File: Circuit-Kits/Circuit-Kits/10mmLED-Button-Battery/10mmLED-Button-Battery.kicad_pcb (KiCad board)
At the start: 2 copper layers, 41.8 x 34.2 mm, 9 parts, among them SW1 Pushbutton

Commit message: Release 10mmLED version 1.0.
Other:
- board text added: "Assembly Information 10mmLED-Button-Battery v1.3"
- board text removed: "Assembly Information LegoLED-Button-Battery v1.3"
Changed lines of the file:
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@@
     (effects (font (size 1.016 1.016) (thickness 0.1524)) (justify right))
   )
-  (gr_text "Assembly Information\nLegoLED-Button-Battery v1.3" (at 185.6232 81.6864) (layer F.Fab)
+  (gr_text "Assembly Information\n10mmLED-Button-Battery v1.3" (at 185.6232 81.6864) (layer F.Fab)
     (effects (font (size 1.016 1.016) (thickness 0.1524)) (justify right))
   )

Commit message: Release USB-Breakout-with-Reset v1.0 fix.
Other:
- board text added: "Crazy Circuit Kit 12/27/16"
- board text removed: "Rewire Circuit Kit 12/27/16"
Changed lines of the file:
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@@
   (gr_line (start 171.6024 114.554) (end 171.6024 115.3668) (layer Edge.Cuts) (width 0.1524))
   (gr_arc (start 175.26 115.316) (end 175.26 118.999) (angle 89.2151803) (layer Edge.Cuts) (width 0.1524))
-  (gr_text "Rewire Circuit Kit\n12/27/16" (at 185.6232 122.428) (layer F.Fab)
+  (gr_text "Crazy Circuit Kit\n12/27/16" (at 185.6232 122.428) (layer F.Fab)
     (effects (font (size 1.016 1.016) (thickness 0.1524)) (justify right))
   )

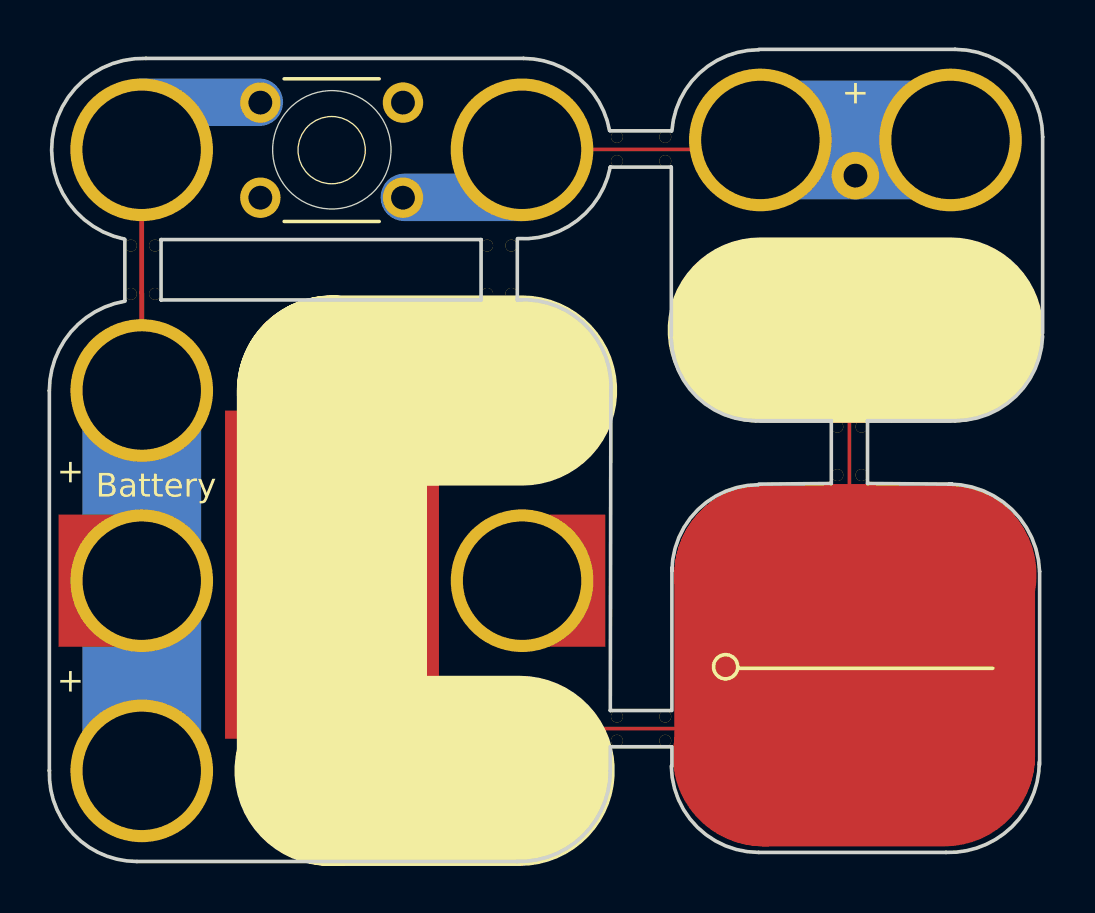
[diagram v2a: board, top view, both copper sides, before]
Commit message: Changed 10mm from 5mm pitch to 2.54mm pitch.
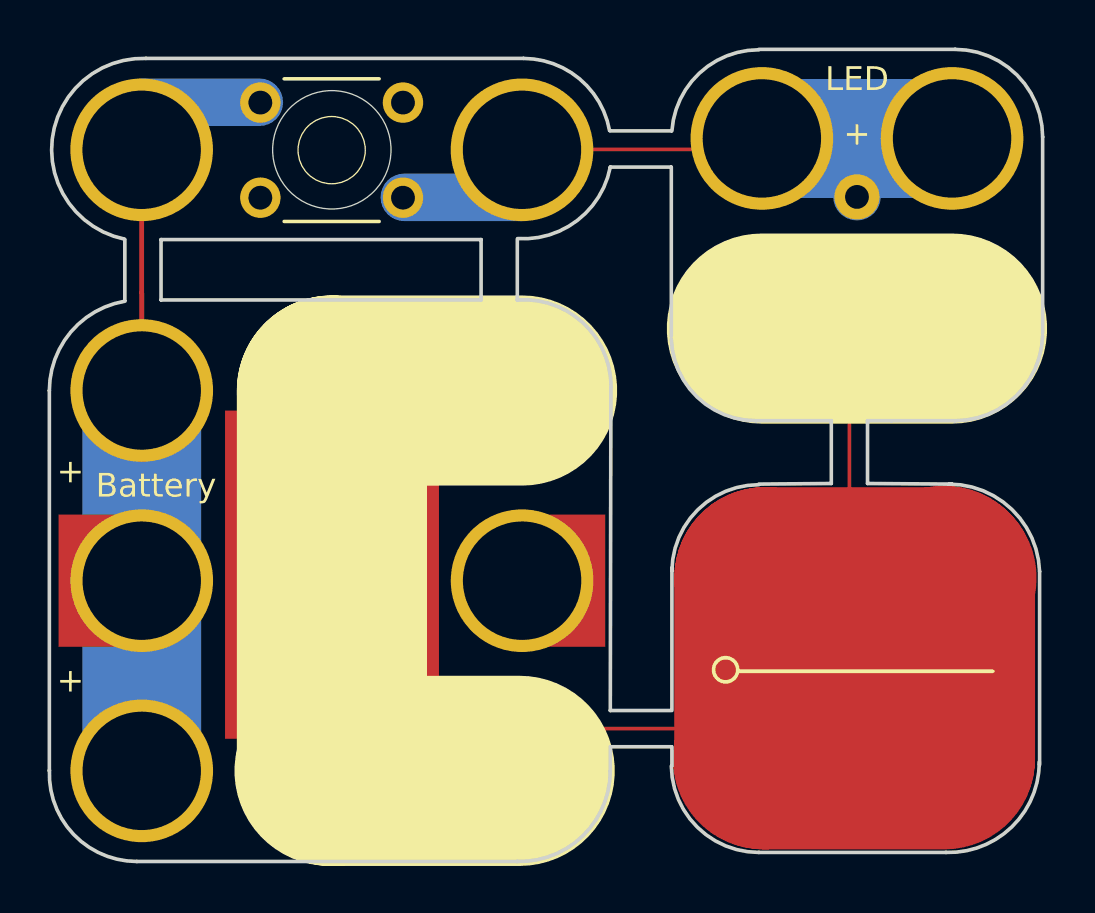
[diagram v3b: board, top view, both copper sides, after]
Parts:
- removed LED: Val**, Crazy_Circuits:LED-10MMD-5MMP-TH-2x2
- removed REF** (x4): TAB-20MIL-2x4-SNAP, Rewire_Circuits:TAB-20MIL-2x2-SNAP
- removed REF**: TAB-20MIL-2x2-SNAP, Rewire_Circuits:TAB-20MIL-2x2-SNAP
- added LED1: LED, Crazy_Circuits:LED-5MMD-2.5MMP-2x2, F.Cu at (183.4, 89.0)
- BT1: footprint Rewire_Circuits:CR2032-3x3-NO-ROTATE -> Crazy_Circuits:CR2032-3x3-NO-ROTATE
- SW1: footprint Rewire_Circuits:BUTTON-1x3-TH-OMRON-B3F-1XXX -> Crazy_Circuits:BUTTON-1x3-TH-OMRON-B3F-1XXX
- moved LOGO 0.13 mm to (179.3, 111.4)
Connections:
- net Net-(BT1-Pad+) renamed +3V
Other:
- board text added: "Assembly Information 10mmLED-Button-Battery v1.1"
- board text added: "Crazy Circuit Kit 1/12/17"
- board text removed: "Assembly Information 10mmLED-Button-Battery v1.3"
- board text removed: "Crazy Circuit Kit 12/27/16"

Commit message: Updated Circuit Kits.
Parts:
- added REF**: TAB-20MIL-2x4-SNAP, Crazy_Circuits:TAB-20MIL-2x2-SNAP, F.Cu at (59.5, 48.0)
- added REF**: TAB-20MIL-2x4-SNAP, Crazy_Circuits:TAB-20MIL-2x2-SNAP, F.Cu at (50.8, 59.7)
- added REF**: TAB-20MIL-2x4-SNAP, Crazy_Circuits:TAB-20MIL-2x2-SNAP, F.Cu at (29.8, 40.3)
- added REF**: TAB-20MIL-2x4-SNAP, Crazy_Circuits:TAB-20MIL-2x2-SNAP, F.Cu at (44.8, 40.3)
- added REF**: TAB-20MIL-2x4-SNAP, Crazy_Circuits:TAB-20MIL-2x2-SNAP, F.Cu at (50.8, 35.3)
- BT1: footprint Crazy_Circuits:CR2032-3x3-NO-ROTATE -> Crazy_Circuits:CR2032-3x3
- LED1: footprint Crazy_Circuits:LED-5MMD-2.5MMP-2x2 -> Crazy_Circuits:LED-2.54MM-TH-2x2
- moved LOGO 131.2 mm to (59.8, 57.2)
- moved BT1 131.2 mm to (45.8, 45.4)
- moved LED1 131.2 mm to (63.9, 34.8)
- moved SW1 131.2 mm to (29.8, 35.3)
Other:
- board text added: "Assembly Information 10mmLED-Button-Battery v1.2"
- board text added: "FABRICATION NOTES 1. THIS IS A 2 LAYER BOARD. 2. EXTERNAL LAYERS SHALL HAVE 1 OZ COPPER. 3. MATERIAL: FR4 AND 0.062 INCH +/- 10% THICK. 4. BOARDS SHALL BE ROHS COMPLIANT. 5. MANUFACTURE IN ACCORDANCE WITH IPC-6012 CLASS 2 6. MASK: BOTH SIDES OF THE BOARD SHALL HAVE SOLDER MASK (ANY COLOR) OVER BARE COPPER. 7. SILK: BOTH SIDES OF THE BOARD SHALL HAVE WHITE SILK. DO NOT PLACE SILK OVER BARE COPPER.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"
- board text removed: "Assembly Information 10mmLED-Button-Battery v1.1"
- board text removed: "Crazy Circuit Kit 1/12/17"

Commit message: Wave solder fixes for v1.3 10mmLED-Button-Battery kit
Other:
- board text removed: "Assembly Information 10mmLED-Button-Battery v1.2"
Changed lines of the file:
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@@
-(kicad_pcb (version 4) (host pcbnew 4.0.5-e0-6337~49~ubuntu16.04.1)
+(kicad_pcb (version 4) (host pcbnew 4.0.7-e2-6376~58~ubuntu16.04.1)
   (general
     (links 16)
     (no_connects 13)
-    (area 21.073553 25.908 68.258248 68.410647)
+    (area 21.073553 25.908 167.965359 182.0418)
     (thickness 1.6)
-    (drawings 48)
+    (drawings 47)
     (tracks 22)
     (zones 0)
@@
     (pad 1 thru_hole circle (at -0.508 1.016 180) (size 0.5 0.5) (drill 0.5) (layers *.Cu))
   )
-  (module Crazy_Circuits:LED-2.54MM-TH-2x2 (layer F.Cu)
-    (at 63.8556 34.8107 180)
-    (descr "LED 5mm round vertical")
-    (tags "LED 5mm round vertical")
-    (fp_text reference LED1 (at 4 -4 270) (layer F.Fab)
-      (effects (font (size 1 1) (thickness 0.15)))
-    )
-    (fp_text value LED (at 4 2.5 180) (layer F.SilkS)
-      (effects (font (size 1 1) (thickness 0.15)))
-    )
-    (fp_line (start 3.302 -7.366) (end 4.445 -7.366) (layer F.Fab) (width 0.0762))
-    (fp_arc (start 3.937 -3.81) (end 5.588 -6.731) (angle 301.0482285) (layer F.Fab) (width 0.0464))
-    (fp_line (start 2.286 -6.731) (end 5.588 -6.731) (layer F.Fab) (width 0.0464))
-    (fp_arc (start 0.195441 -0.199792) (end 0 3.8) (angle 84.2) (layer Edge.Cuts) (width 0.05))
-    (fp_line (start 11.8 -8) (end 11.8 0) (layer Edge.Cuts) (width 0.05))
-    (fp_line (start 0 -11.8) (end 8 -11.8) (layer Edge.Cuts) (width 0.05))
-    (fp_line (start 0 3.8) (end 8 3.8) (layer Edge.Cuts) (width 0.05))
-    (fp_line (start -3.8 -8) (end -3.8 0) (layer Edge.Cuts) (width 0.05))
-    (fp_arc (start 0.195441 -0.199792) (end 0 3.8) (angle 84.2) (layer F.Fab) (width 0.05))
-    (fp_line (start 11.8 -8) (end 11.8 0) (layer F.Fab) (width 0.05))
-    (fp_line (start 0 -11.8) (end 8 -11.8) (layer F.Fab) (width 0.05))
-    (fp_line (start 0 3.8) (end 8 3.8) (layer F.Fab) (width 0.05))
-    (fp_line (start -3.8 -8) (end -3.8 0) (layer F.Fab) (width 0.05))
-    (fp_line (start 4 -5.2) (end 4 -6.3) (layer B.Cu) (width 2))
-    (fp_line (start 8 -8) (end 0 -8) (layer B.Mask) (width 7))
-    (fp_text user + (at 4 0.2 180) (layer F.SilkS)
-      (effects (font (size 1 1) (thickness 0.15)))
-    )
-    (fp_line (start 0 -8) (end 8 -8) (layer F.SilkS) (width 8))
-    (fp_line (start 2.5 -6.23) (end 5.5 -6.23) (layer F.SilkS) (width 0.15))
-    (fp_line (start 8 -8) (end 0 -8) (layer B.Cu) (width 7))
-    (fp_line (start 8 0) (end 0 0) (layer B.Mask) (width 7))
-    (fp_line (start 8 0) (end 0 0) (layer B.Cu) (width 7))
-    (fp_line (start 4 -1.35) (end 4 -2.45) (layer B.Cu) (width 2))
-    (fp_arc (start 7.800208 -0.195441) (end 11.8 0) (angle 84.2) (layer Edge.Cuts) (width 0.05))
-    (fp_arc (start 0.199792 -7.804559) (end -3.8 -8) (angle 84.2) (layer Edge.Cuts) (width 0.05))
-    (fp_arc (start 7.804559 -7.800208) (end 8 -11.8) (angle 84.2) (layer Edge.Cuts) (width 0.05))
-    (fp_arc (start 7.800208 -0.195441) (end 11.8 0) (angle 84.2) (layer F.Fab) (width 0.05))
-    (fp_arc (start 0.199792 -7.804559) (end -3.8 -8) (angle 84.2) (layer F.Fab) (width 0.05))
-    (fp_arc (start 7.804559 -7.800208) (end 8 -11.8) (angle 84.2) (layer F.Fab) (width 0.05))
-    (fp_line (start 3.683 0.635) (end 4.699 0.635) (layer F.Fab) (width 0.127))
-    (fp_line (start 4.191 1.2065) (end 4.191 0.0635) (layer F.Fab) (width 0.127))
-    (pad - thru_hole rect (at 4 -5 180) (size 2 1.9) (drill 1.00076) (layers *.Cu *.Mask)
-      (net 1 GND))
-    (pad + thru_hole circle (at 4 -2.46 90) (size 1.9 1.9) (drill 1.00076) (layers *.Cu *.Mask)
-      (net 2 "Net-(LED1-Pad+)"))
-    (pad + thru_hole circle (at 0 0 180) (size 6 6) (drill 4.98) (layers *.Cu B.Mask)
-      (net 2 "Net-(LED1-Pad+)"))
-    (pad - thru_hole circle (at 0 -8 180) (size 6 6) (drill 4.98) (layers *.Cu B.Mask)
-      (net 1 GND))
-    (pad - thru_hole circle (at 8 -8 180) (size 6 6) (drill 4.98) (layers *.Cu B.Mask)
-      (net 1 GND))
-    (pad + thru_hole circle (at 8 0 180) (size 6 6) (drill 4.98) (layers *.Cu B.Mask)
-      (net 2 "Net-(LED1-Pad+)"))
-  )
   (module Crazy_Circuits:BUTTON-1x3-TH-OMRON-B3F-1XXX (layer F.Cu)
     (at 29.764801 35.289601)
@@
     (pad 1 thru_hole circle (at -0.508 1.016 90) (size 0.5 0.5) (drill 0.5) (layers *.Cu))
   )
+  (module Crazy_Circuits:LED-2.54MM-TH-2x2 (layer F.Cu)
+    (at 63.8556 34.8107 180)
+    (descr "LED 5mm round vertical")
+    (tags "LED 5mm round vertical")
+    (fp_text reference LED1 (at 4 -4 270) (layer F.Fab)
+      (effects (font (size 1 1) (thickness 0.15)))
+    )
+    (fp_text value LED (at 4 2.5 180) (layer F.SilkS)
+      (effects (font (size 1 1) (thickness 0.15)))
+    )
+    (fp_line (start 8.001 -9.4996) (end 0.0254 -9.4996) (layer B.Mask) (width 4))
+    (fp_arc (start 7.9756 0) (end 8.001 -2.9718) (angle 269.5103044) (layer B.Mask) (width 1))
+    (fp_line (start 3.302 -7.366) (end 4.445 -7.366) (layer F.Fab) (width 0.0762))
+    (fp_arc (start 3.937 -3.81) (end 5.588 -6.731) (angle 301.0482285) (layer F.Fab) (width 0.0464))
+    (fp_line (start 2.286 -6.731) (end 5.588 -6.731) (layer F.Fab) (width 0.0464))
+    (fp_arc (start 0.195441 -0.199792) (end 0 3.8) (angle 84.2) (layer Edge.Cuts) (width 0.05))
+    (fp_line (start 11.8 -8) (end 11.8 0) (layer Edge.Cuts) (width 0.05))
+    (fp_line (start 0 -11.8) (end 8 -11.8) (layer Edge.Cuts) (width 0.05))
+    (fp_line (start 0 3.8) (end 8 3.8) (layer Edge.Cuts) (width 0.05))
+    (fp_line (start -3.8 -8) (end -3.8 0) (layer Edge.Cuts) (width 0.05))
+    (fp_arc (start 0.195441 -0.199792) (end 0 3.8) (angle 84.2) (layer F.Fab) (width 0.05))
+    (fp_line (start 11.8 -8) (end 11.8 0) (layer F.Fab) (width 0.05))
+    (fp_line (start 0 -11.8) (end 8 -11.8) (layer F.Fab) (width 0.05))
+    (fp_line (start 0 3.8) (end 8 3.8) (layer F.Fab) (width 0.05))
+    (fp_line (start -3.8 -8) (end -3.8 0) (layer F.Fab) (width 0.05))
+    (fp_line (start 4 -5.2) (end 4 -6.3) (layer B.Cu) (width 2))
+    (fp_text user + (at 4 0.2 180) (layer F.SilkS)
+      (effects (font (size 1 1) (thickness 0.15)))
+    )
+    (fp_line (start 0 -8) (end 8 -8) (layer F.SilkS) (width 8))
+    (fp_line (start 2.5 -6.23) (end 5.5 -6.23) (layer F.SilkS) (width 0.15))
+    (fp_line (start 8 -8) (end 0 -8) (layer B.Cu) (width 7))
+    (fp_line (start 8 0) (end 0 0) (layer B.Cu) (width 7))
+    (fp_line (start 4 -1.35) (end 4 -2.45) (layer B.Cu) (width 2))
+    (fp_arc (start 7.800208 -0.195441) (end 11.8 0) (angle 84.2) (layer Edge.Cuts) (width 0.05))
+    (fp_arc (start 0.199792 -7.804559) (end -3.8 -8) (angle 84.2) (layer Edge.Cuts) (width 0.05))
+    (fp_arc (start 7.804559 -7.800208) (end 8 -11.8) (angle 84.2) (layer Edge.Cuts) (width 0.05))
+    (fp_arc (start 7.800208 -0.195441) (end 11.8 0) (angle 84.2) (layer F.Fab) (width 0.05))
+    (fp_arc (start 0.199792 -7.804559) (end -3.8 -8) (angle 84.2) (layer F.Fab) (width 0.05))
+    (fp_arc (start 7.804559 -7.800208) (end 8 -11.8) (angle 84.2) (layer F.Fab) (width 0.05))
+    (fp_line (start 3.683 0.635) (end 4.699 0.635) (layer F.Fab) (width 0.127))
+    (fp_line (start 4.191 1.2065) (end 4.191 0.0635) (layer F.Fab) (width 0.127))
+    (fp_arc (start -0.0254 0) (end 2.9464 0.0254) (angle 269.5103044) (layer B.Mask) (width 1))
+    (fp_arc (start 8.001 -8.0264) (end 5.0292 -8.0518) (angle 269.5103044) (layer B.Mask) (width 1))
+    (fp_arc (start 0 -8.0264) (end -0.0254 -5.0546) (angle 269.5103044) (layer B.Mask) (width 1))
+    (fp_line (start 8.255 1.4732) (end 0.2794 1.4732) (layer B.Mask) (width 4))
+    (pad - thru_hole circle (at 4 -5 180) (size 2 2) (drill 1.00076) (layers *.Cu *.Mask)
+      (net 1 GND))
+    (pad + thru_hole circle (at 4 -2.46 90) (size 1.9 1.9) (drill 1.00076) (layers *.Cu *.Mask)
+      (net 2 "Net-(LED1-Pad+)"))
+    (pad + thru_hole circle (at 0 0 180) (size 6 6) (drill 4.98) (layers *.Cu F.Mask)
+      (net 2 "Net-(LED1-Pad+)"))
+    (pad - thru_hole circle (at 0 -8 180) (size 6 6) (drill 4.98) (layers *.Cu F.Mask)
+      (net 1 GND))
+    (pad - thru_hole circle (at 8 -8 180) (size 6 6) (drill 4.98) (layers *.Cu F.Mask)
+      (net 1 GND))
+    (pad + thru_hole circle (at 8 0 180) (size 6 6) (drill 4.98) (layers *.Cu F.Mask)
+      (net 2 "Net-(LED1-Pad+)"))
+  )
   (gr_text "FABRICATION NOTES\n\n1. THIS IS A 2 LAYER BOARD. \n2. EXTERNAL LAYERS SHALL HAVE 1 OZ COPPER.\n3. MATERIAL: FR4 AND 0.062 INCH +/- 10% THICK.\n4. BOARDS SHALL BE ROHS COMPLIANT. \n5. MANUFACTURE IN ACCORDANCE WITH IPC-6012 CLASS 2\n6. MASK: BOTH SIDES OF THE BOARD SHALL HAVE \n   SOLDER MASK (ANY COLOR) OVER BARE COPPER. \n7. SILK: BOTH SIDES OF THE BOARD SHALL HAVE WHITE SILK. \n   DO NOT PLACE SILK OVER BARE COPPER.\n8. FINISH: ENIG.\n9. MINIMUM TRACE WIDTH - 0.006 INCH.\n   MINIMUM SPACE - 0.006 INCH.\n   MINIMUM HOLE DIA - 0.013 INCH. \n10. MAX HOLE PLACEMENT TOLERANCE OF +/- 0.003 INCH.\n11. MAX HOLE DIAMETER TOLERANCE OF +/- 0.003 INCH AFTER PLATING." (at 25.1206 147.3708) (layer Dwgs.User)
     (effects (font (size 2.54 2.54) (thickness 0.254)) (justify left))
@@
   (gr_line (start 52.07 60.4012) (end 52.07 61.214) (layer Edge.Cuts) (width 0.1524))
   (gr_arc (start 55.7276 61.1632) (end 55.7276 64.8462) (angle 89.2151803) (layer Edge.Cuts) (width 0.1524))
-  (gr_text "Assembly Information\n10mmLED-Button-Battery v1.2" (at 66.0908 27.5336) (layer F.Fab)
-    (effects (font (size 1.016 1.016) (thickness 0.1524)) (justify right))
-  )
   (gr_line (start 60.2996 46.6852) (end 61.3156 46.6852) (layer Edge.Cuts) (width 0.1524))
   (gr_line (start 49.4792 60.4012) (end 49.4792 61.4172) (layer Edge.Cuts) (width 0.1524))
